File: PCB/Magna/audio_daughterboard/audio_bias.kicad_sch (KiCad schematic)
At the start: 8 parts, among them U801 NE5532

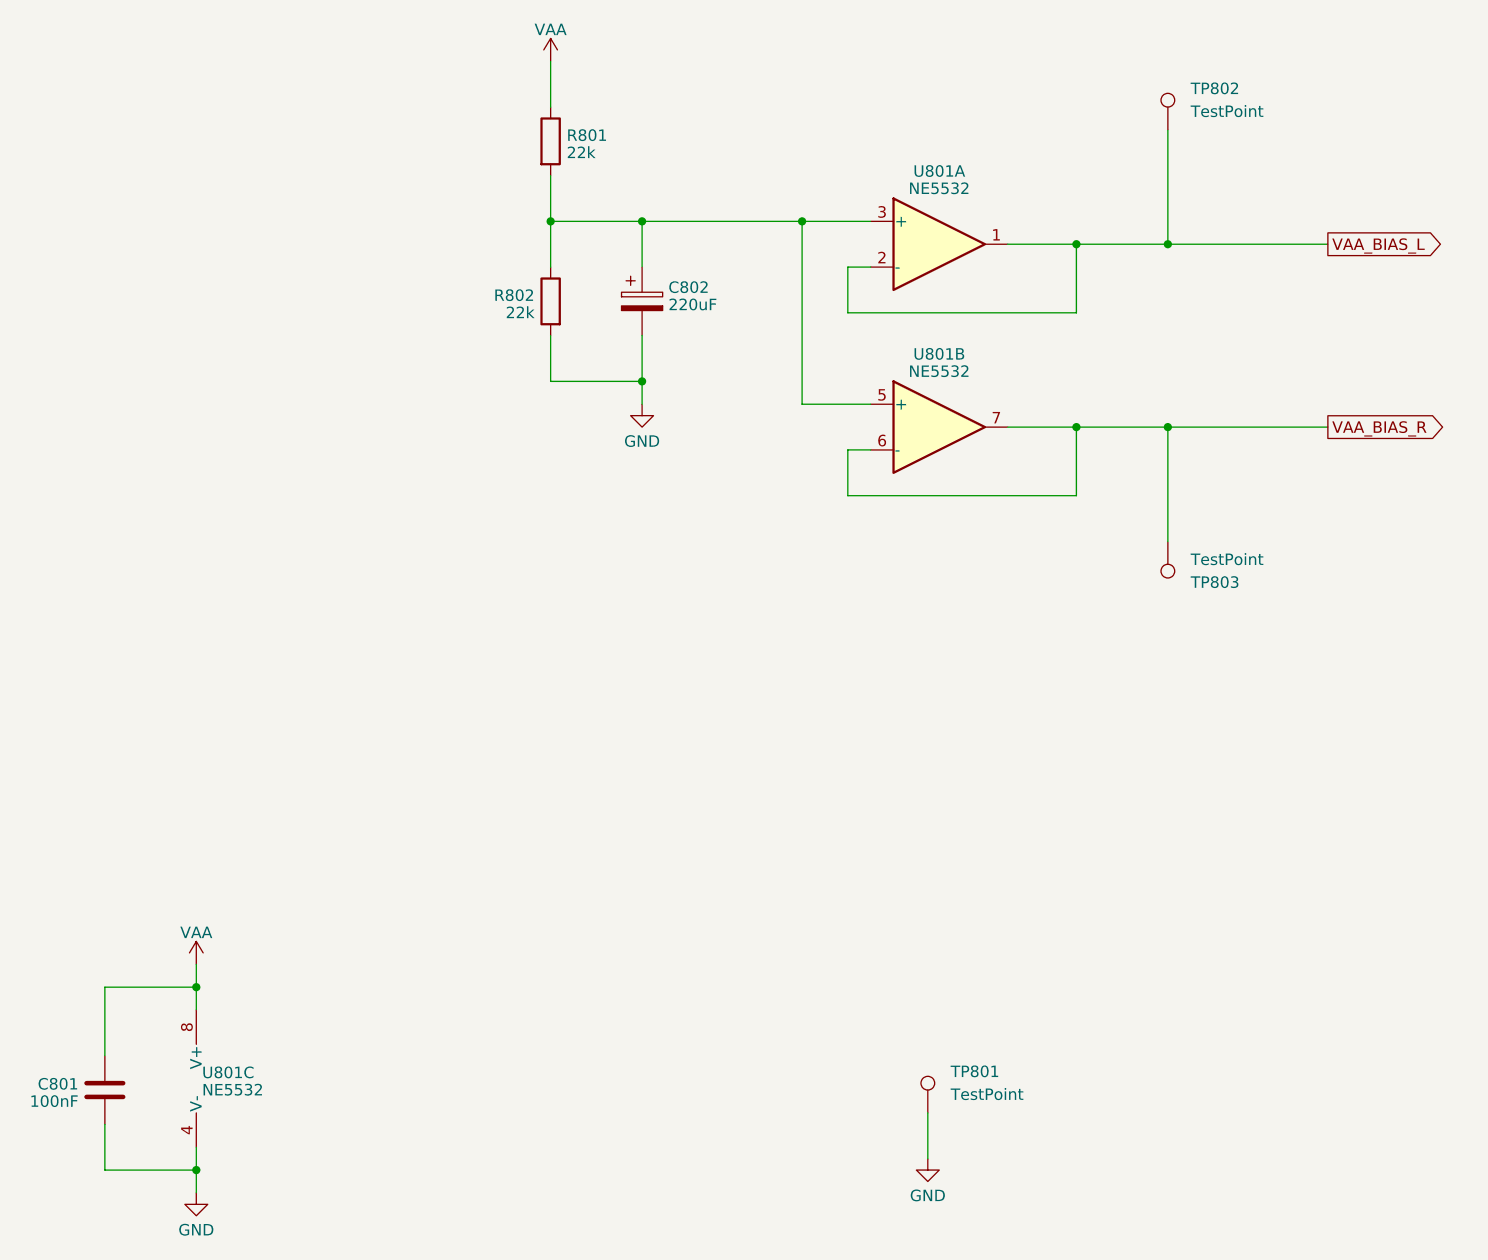
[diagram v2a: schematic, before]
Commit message: Start layout and routing of Audio Daugherboard
Also a lot of small changes to everything that became apperant
when the audio daughterboard was designed. Such as the Headphone
PCB, which is now separate from the rest of the audio.
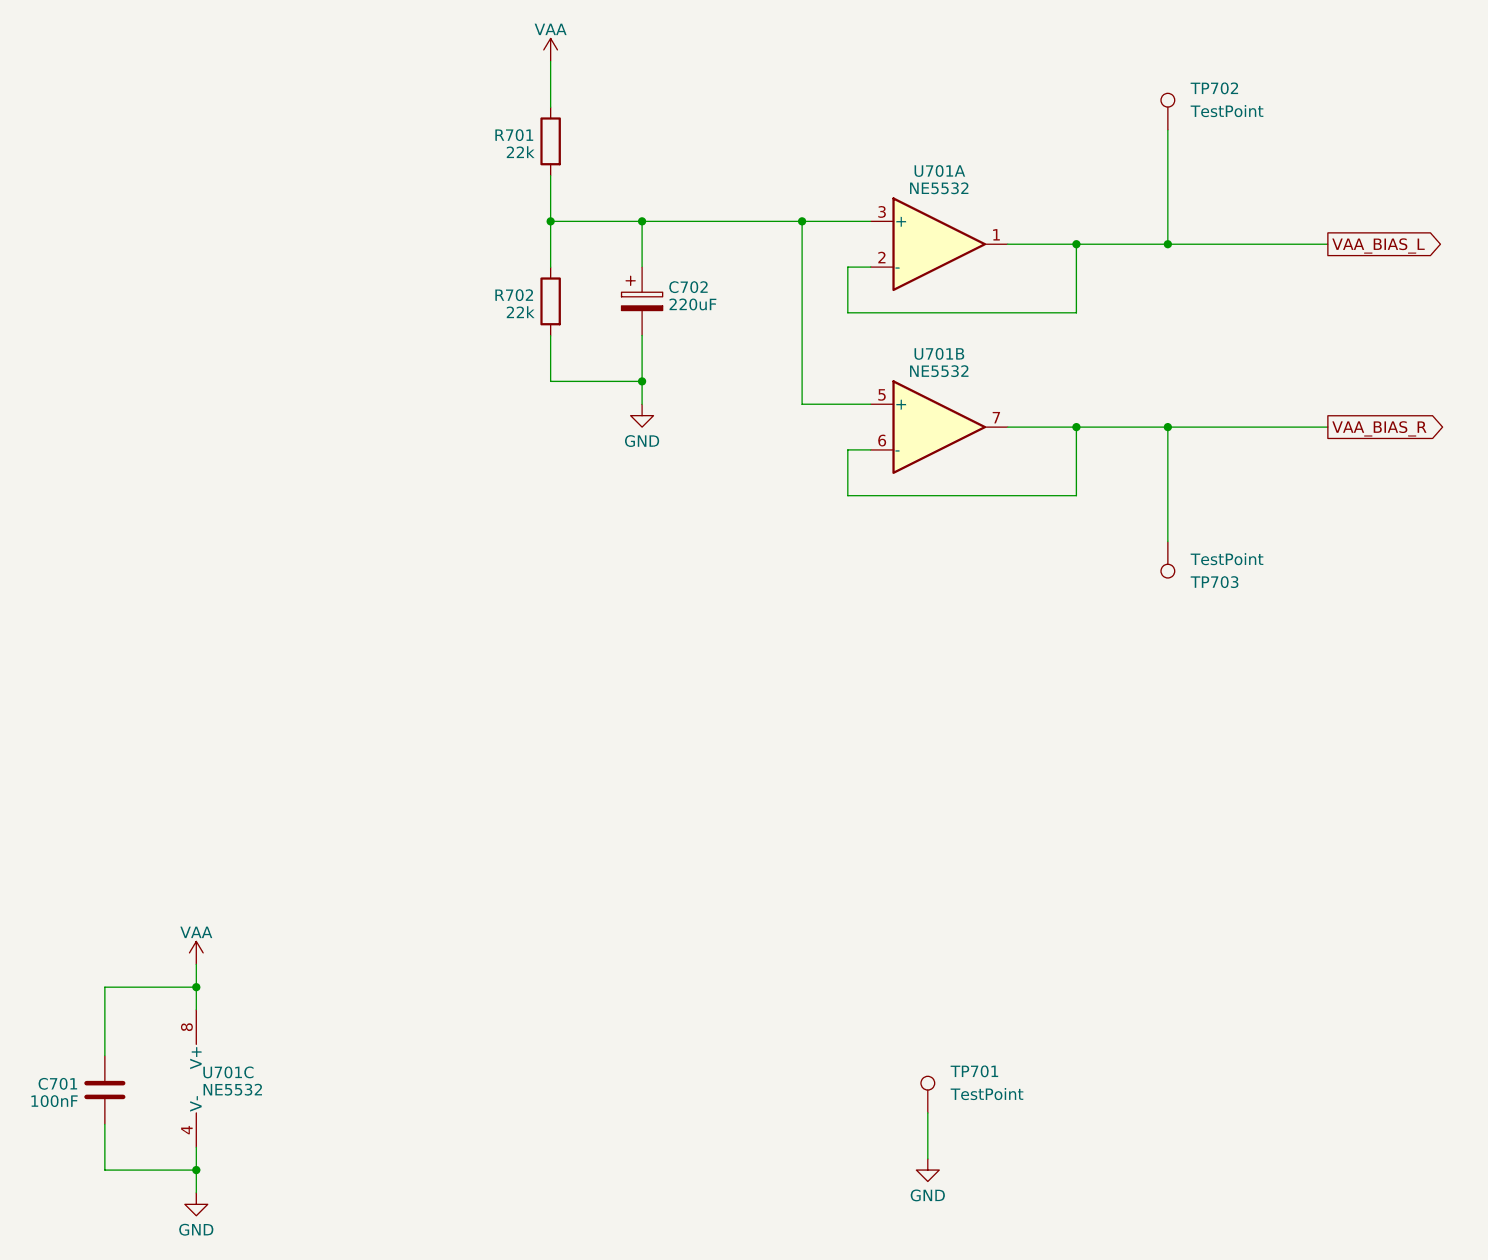
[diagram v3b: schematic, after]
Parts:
- renumbered C801 to C701, C802 to C702, R801 to R701, R802 to R702, TP801 to TP701, TP802 to TP702, TP803 to TP703, U801 to U701
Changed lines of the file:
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@@
 		(dnp no)
 		(fields_autoplaced yes)
-		(property "Reference" "#PWR0803"
+		(property "Reference" "#PWR0703"
 			(at 100.33 60.96 0)
 			(effects
@@
 			(project "Audio_daughterboard"
 				(path "/1eadd930-2484-4c28-b568-78e6454e7f52/eddc896c-2eca-4cc9-a7eb-0b3af1aefe11"
-					(reference "#PWR0803")
+					(reference "#PWR0703")
 					(unit 1)
 				)
@@
 		(dnp no)
 		(fields_autoplaced yes)
-		(property "Reference" "#PWR0804"
+		(property "Reference" "#PWR0704"
 			(at 110.49 101.6 0)
 			(effects
@@
 			(project "Audio_daughterboard"
 				(path "/1eadd930-2484-4c28-b568-78e6454e7f52/eddc896c-2eca-4cc9-a7eb-0b3af1aefe11"
-					(reference "#PWR0804")
+					(reference "#PWR0704")
 					(unit 1)
 				)
@@
 		(dnp no)
 		(fields_autoplaced yes)
-		(property "Reference" "TP803"
+		(property "Reference" "TP703"
 			(at 171.45 115.062 0)
 			(effects
@@
 			(project "Audio_daughterboard"
 				(path "/1eadd930-2484-4c28-b568-78e6454e7f52/eddc896c-2eca-4cc9-a7eb-0b3af1aefe11"
-					(reference "TP803")
+					(reference "TP703")
 					(unit 1)
 				)
@@
 		(dnp no)
 		(fields_autoplaced yes)
-		(property "Reference" "#PWR0801"
+		(property "Reference" "#PWR0701"
 			(at 60.96 161.29 0)
 			(effects
@@
 			(project "Audio_daughterboard"
 				(path "/1eadd930-2484-4c28-b568-78e6454e7f52/eddc896c-2eca-4cc9-a7eb-0b3af1aefe11"
-					(reference "#PWR0801")
+					(reference "#PWR0701")
 					(unit 1)
 				)
@@
 		(lib_id "Device:R")
 		(at 100.33 66.04 0)
+		(mirror y)
 		(unit 1)
 		(exclude_from_sim no)
@@
 		(on_board yes)
 		(dnp no)
-		(fields_autoplaced yes)
-		(property "Reference" "R801"
-			(at 102.108 65.3963 0)
+		(property "Reference" "R701"
+			(at 98.552 65.3963 0)
 			(effects
 				(font
@@
 		)
 		(property "Value" "22k"
-			(at 102.108 67.3173 0)
+			(at 98.552 67.3173 0)
 			(effects
 				(font
@@
 		)
 		(property "Footprint" "Resistor_SMD:R_0603_1608Metric"
-			(at 98.552 66.04 90)
+			(at 102.108 66.04 90)
 			(effects
 				(font
@@
 			(project "Audio_daughterboard"
 				(path "/1eadd930-2484-4c28-b568-78e6454e7f52/eddc896c-2eca-4cc9-a7eb-0b3af1aefe11"
-					(reference "R801")
+					(reference "R701")
 					(unit 1)
 				)
@@
 		(dnp no)
 		(fields_autoplaced yes)
-		(property "Reference" "U801"
+		(property "Reference" "U701"
 			(at 143.51 89.7001 0)
 			(effects
@@
 			(project "Audio_daughterboard"
 				(path "/1eadd930-2484-4c28-b568-78e6454e7f52/eddc896c-2eca-4cc9-a7eb-0b3af1aefe11"
-					(reference "U801")
+					(reference "U701")
 					(unit 2)
 				)
@@
 		(dnp no)
 		(fields_autoplaced yes)
-		(property "Reference" "U801"
+		(property "Reference" "U701"
 			(at 61.595 169.5363 0)
 			(effects
@@
 			(project "Audio_daughterboard"
 				(path "/1eadd930-2484-4c28-b568-78e6454e7f52/eddc896c-2eca-4cc9-a7eb-0b3af1aefe11"
-					(reference "U801")
+					(reference "U701")
 					(unit 3)
 				)
@@
 		(dnp no)
 		(fields_autoplaced yes)
-		(property "Reference" "U801"
+		(property "Reference" "U701"
 			(at 143.51 69.3801 0)
 			(effects
@@
 			(project "Audio_daughterboard"
 				(path "/1eadd930-2484-4c28-b568-78e6454e7f52/eddc896c-2eca-4cc9-a7eb-0b3af1aefe11"
-					(reference "U801")
+					(reference "U701")
 					(unit 1)
 				)
@@
 		(dnp no)
 		(fields_autoplaced yes)
-		(property "Reference" "R802"
+		(property "Reference" "R702"
 			(at 98.552 83.1763 0)
 			(effects
@@
 			(project "Audio_daughterboard"
 				(path "/1eadd930-2484-4c28-b568-78e6454e7f52/eddc896c-2eca-4cc9-a7eb-0b3af1aefe11"
-					(reference "R802")
+					(reference "R702")
 					(unit 1)
 				)
@@
 		(dnp no)
 		(fields_autoplaced yes)
-		(property "Reference" "TP801"
+		(property "Reference" "TP701"
 			(at 144.78 169.418 0)
 			(effects
@@
 			(project "Audio_daughterboard"
 				(path "/1eadd930-2484-4c28-b568-78e6454e7f52/eddc896c-2eca-4cc9-a7eb-0b3af1aefe11"
-					(reference "TP801")
+					(reference "TP701")
 					(unit 1)
 				)
@@
 		(on_board yes)
 		(dnp no)
-		(property "Reference" "C802"
+		(property "Reference" "C702"
 			(at 113.411 82.2873 0)
 			(effects
@@
 			(project "Audio_daughterboard"
 				(path "/1eadd930-2484-4c28-b568-78e6454e7f52/eddc896c-2eca-4cc9-a7eb-0b3af1aefe11"
-					(reference "C802")
+					(reference "C702")
 					(unit 1)
 				)
@@
 		(dnp no)
 		(fields_autoplaced yes)
-		(property "Reference" "TP802"
+		(property "Reference" "TP702"
 			(at 171.45 60.198 0)
 			(effects
@@
 			(project "Audio_daughterboard"
 				(path "/1eadd930-2484-4c28-b568-78e6454e7f52/eddc896c-2eca-4cc9-a7eb-0b3af1aefe11"
-					(reference "TP802")
+					(reference "TP702")
 					(unit 1)
 				)
@@
 		(on_board yes)
 		(dnp no)
-		(property "Reference" "C801"
+		(property "Reference" "C701"
 			(at 47.879 170.8063 0)
 			(effects
@@
 			(project "Audio_daughterboard"
 				(path "/1eadd930-2484-4c28-b568-78e6454e7f52/eddc896c-2eca-4cc9-a7eb-0b3af1aefe11"
-					(reference "C801")
+					(reference "C701")
 					(unit 1)
 				)
@@
 		(dnp no)
 		(fields_autoplaced yes)
-		(property "Reference" "#PWR0802"
+		(property "Reference" "#PWR0702"
 			(at 60.96 189.23 0)
 			(effects
@@
 			(project "Audio_daughterboard"
 				(path "/1eadd930-2484-4c28-b568-78e6454e7f52/eddc896c-2eca-4cc9-a7eb-0b3af1aefe11"
-					(reference "#PWR0802")
+					(reference "#PWR0702")
 					(unit 1)
 				)
@@
 		(dnp no)
 		(fields_autoplaced yes)
-		(property "Reference" "#PWR0805"
+		(property "Reference" "#PWR0705"
 			(at 142.24 185.42 0)
 			(effects
@@
 			(project "Audio_daughterboard"
 				(path "/1eadd930-2484-4c28-b568-78e6454e7f52/eddc896c-2eca-4cc9-a7eb-0b3af1aefe11"
-					(reference "#PWR0805")
-					(unit 1)
-				)
+					(reference "#PWR0705")
+					(unit 1)
+				)

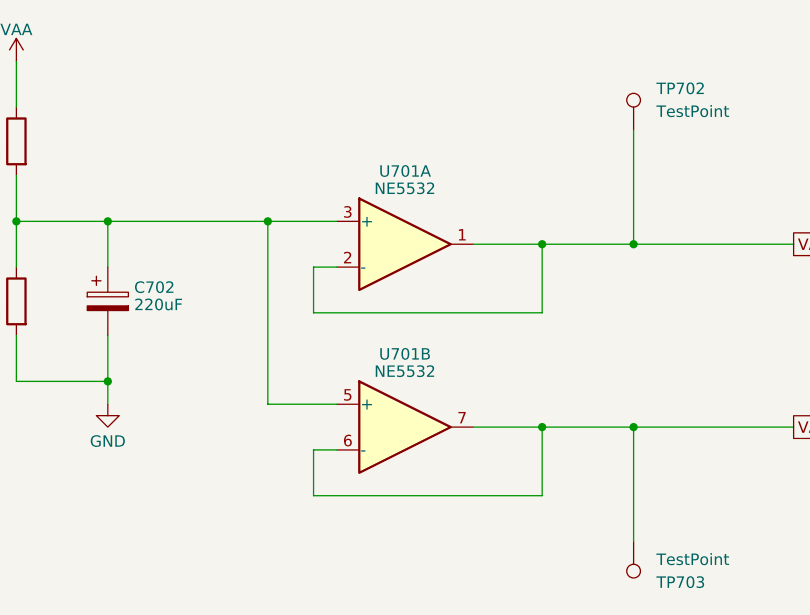
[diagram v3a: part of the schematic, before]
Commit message: Finished first round of routing for the Audio Daughterboard
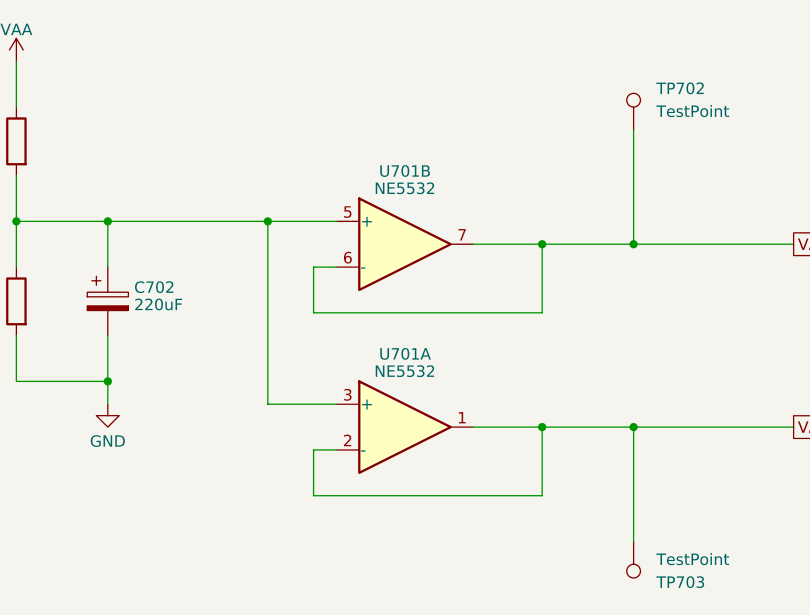
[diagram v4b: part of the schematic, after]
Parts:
- R701, R702: now in the parts list
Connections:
- net VAA_BIAS_L: now also U701.6 (-), U701.7; no longer U701.1, U701.2 (-)
- net VAA_BIAS_R: now also U701.1, U701.2 (-); no longer U701.6 (-), U701.7
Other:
- moved on the sheet: U701A, U701B
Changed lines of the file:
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@@
 		(unit 1)
 		(exclude_from_sim no)
-		(in_bom no)
+		(in_bom yes)
 		(on_board yes)
 		(dnp no)
@@
 	(symbol
 		(lib_id "Amplifier_Operational:NE5532")
-		(at 143.51 97.79 0)
+		(at 143.51 77.47 0)
 		(unit 2)
 		(exclude_from_sim no)
@@
 		(fields_autoplaced yes)
 		(property "Reference" "U701"
-			(at 143.51 89.7001 0)
+			(at 143.51 69.3801 0)
 			(effects
 				(font
@@
 		)
 		(property "Value" "NE5532"
-			(at 143.51 91.6211 0)
+			(at 143.51 71.3011 0)
 			(effects
 				(font
@@
 		)
 		(property "Footprint" "Package_SO:SOIC-8_3.9x4.9mm_P1.27mm"
-			(at 143.51 97.79 0)
+			(at 143.51 77.47 0)
 			(effects
 				(font
@@
 		)
 		(property "Datasheet" "http://www.ti.com/lit/ds/symlink/ne5532.pdf"
-			(at 143.51 97.79 0)
+			(at 143.51 77.47 0)
 			(effects
 				(font
@@
 		)
 		(property "Description" "Dual Low-Noise Operational Amplifiers, DIP-8/SOIC-8"
-			(at 143.51 97.79 0)
+			(at 143.51 77.47 0)
 			(effects
 				(font
@@
 		)
 		(property "LCSC" "C7426"
-			(at 143.51 97.79 0)
+			(at 143.51 77.47 0)
 			(effects
 				(font
@@
 		)
 		(property "Sim.Device" "SUBCKT"
-			(at 143.51 97.79 0)
+			(at 143.51 77.47 0)
 			(effects
 				(font
@@
 		)
 		(property "Sim.Library" "${KICAD7_SYMBOL_DIR}/Simulation_SPICE.sp"
-			(at 143.51 97.79 0)
+			(at 143.51 77.47 0)
 			(effects
 				(font
@@
 		)
 		(property "Sim.Name" "kicad_builtin_opamp_dual"
-			(at 143.51 97.79 0)
+			(at 143.51 77.47 0)
 			(effects
 				(font
@@
 		)
 		(property "Sim.Pins" "1=out1 2=in1- 3=in1+ 4=vee 5=in2+ 6=in2- 7=out2 8=vcc"
-			(at 143.51 97.79 0)
+			(at 143.51 77.47 0)
 			(effects
 				(font
@@
 		)
 		(property "Field5" ""
-			(at 143.51 97.79 0)
+			(at 143.51 77.47 0)
 			(effects
 				(font
@@
 	(symbol
 		(lib_id "Amplifier_Operational:NE5532")
-		(at 143.51 77.47 0)
+		(at 143.51 97.79 0)
 		(unit 1)
 		(exclude_from_sim no)
@@
 		(fields_autoplaced yes)
 		(property "Reference" "U701"
-			(at 143.51 69.3801 0)
+			(at 143.51 89.7001 0)
 			(effects
 				(font
@@
 		)
 		(property "Value" "NE5532"
-			(at 143.51 71.3011 0)
+			(at 143.51 91.6211 0)
 			(effects
 				(font
@@
 		)
 		(property "Footprint" "Package_SO:SOIC-8_3.9x4.9mm_P1.27mm"
-			(at 143.51 77.47 0)
+			(at 143.51 97.79 0)
 			(effects
 				(font
@@
 		)
 		(property "Datasheet" "http://www.ti.com/lit/ds/symlink/ne5532.pdf"
-			(at 143.51 77.47 0)
+			(at 143.51 97.79 0)
 			(effects
 				(font
@@
 		)
 		(property "Description" "Dual Low-Noise Operational Amplifiers, DIP-8/SOIC-8"
-			(at 143.51 77.47 0)
+			(at 143.51 97.79 0)
 			(effects
 				(font
@@
 		)
 		(property "LCSC" "C7426"
-			(at 143.51 77.47 0)
+			(at 143.51 97.79 0)
 			(effects
 				(font
@@
 		)
 		(property "Sim.Device" "SUBCKT"
-			(at 143.51 77.47 0)
+			(at 143.51 97.79 0)
 			(effects
 				(font
@@
 		)
 		(property "Sim.Library" "${KICAD7_SYMBOL_DIR}/Simulation_SPICE.sp"
-			(at 143.51 77.47 0)
+			(at 143.51 97.79 0)
 			(effects
 				(font
@@
 		)
 		(property "Sim.Name" "kicad_builtin_opamp_dual"
-			(at 143.51 77.47 0)
+			(at 143.51 97.79 0)
 			(effects
 				(font
@@
 		)
 		(property "Sim.Pins" "1=out1 2=in1- 3=in1+ 4=vee 5=in2+ 6=in2- 7=out2 8=vcc"
-			(at 143.51 77.47 0)
+			(at 143.51 97.79 0)
 			(effects
 				(font
@@
 		)
 		(property "Field5" ""
-			(at 143.51 77.47 0)
+			(at 143.51 97.79 0)
 			(effects
 				(font
@@
 		(unit 1)
 		(exclude_from_sim no)
-		(in_bom no)
+		(in_bom yes)
 		(on_board yes)
 		(dnp no)
